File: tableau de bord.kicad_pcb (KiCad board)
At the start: 2 copper layers, 36.8 x 42.5 mm, 15 parts, among them J1 TS ON, J2 Alim, J3 R2D, J4 Potentiometre, J5 commande onduleur, U1 L7805

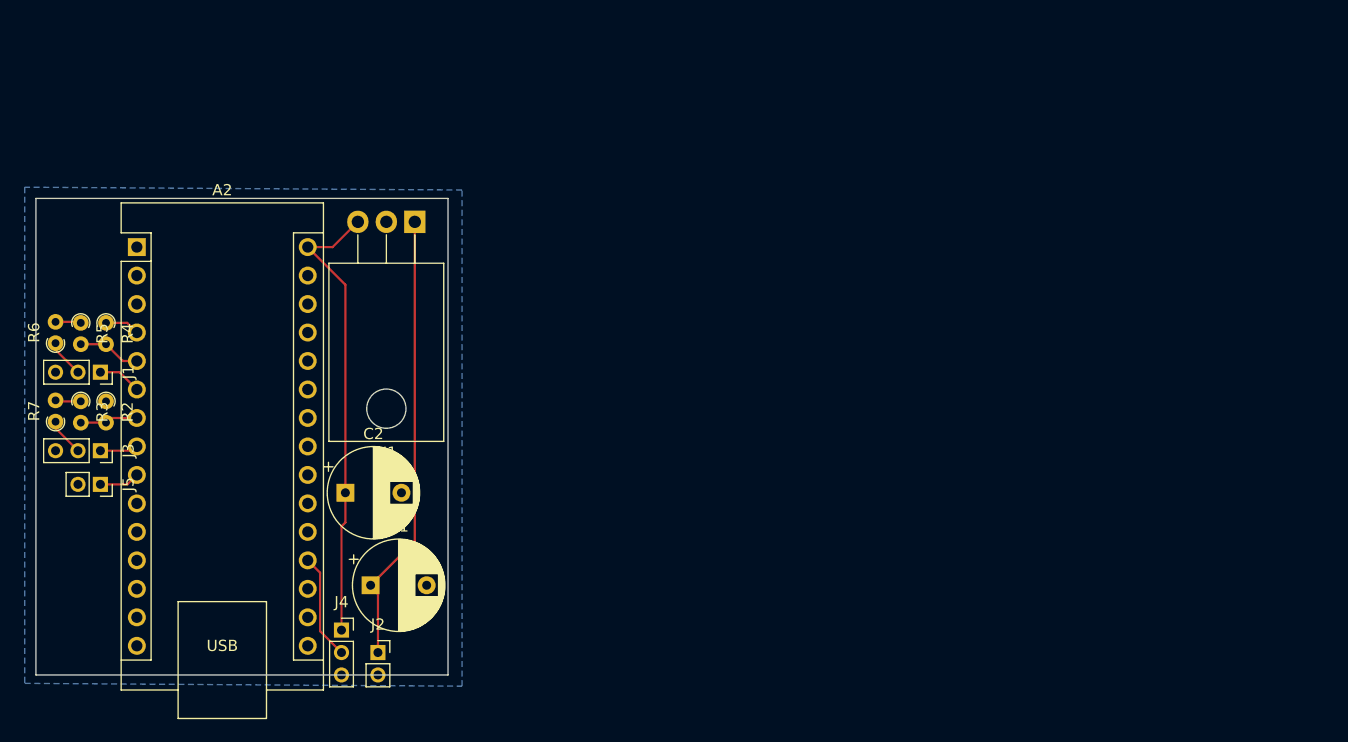
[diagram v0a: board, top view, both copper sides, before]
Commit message: Version 2:
- ajout de mosfet pour commander les relais.
- mise en forme des connecteurs
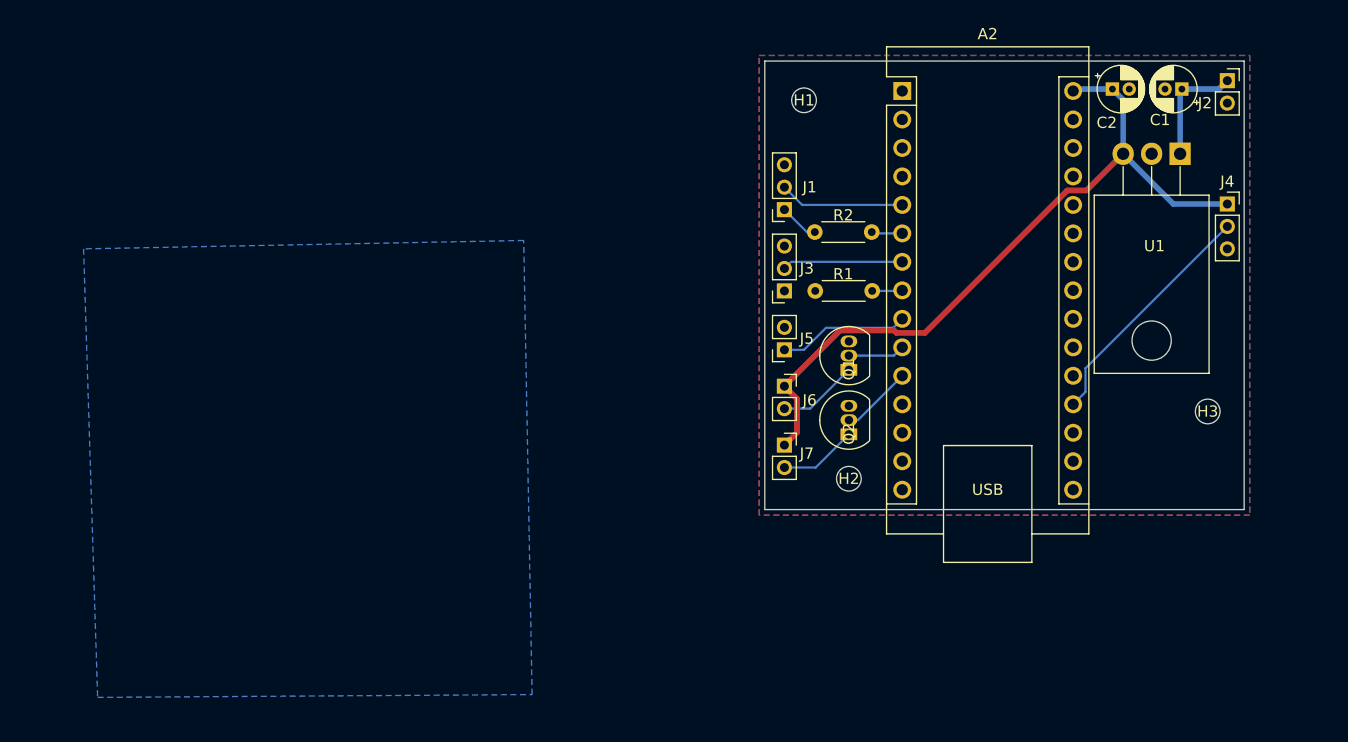
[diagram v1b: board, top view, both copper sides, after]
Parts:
- removed R3, R5: 47k, Resistor_THT:R_Axial_DIN0204_L3.6mm_D1.6mm_P1.90mm_Vertical
- removed R4, R6, R7: 4.7k, Resistor_THT:R_Axial_DIN0204_L3.6mm_D1.6mm_P1.90mm_Vertical
- added H1: MountingHole, MountingHole:MountingHole_2.2mm_M2, F.Cu at (139.5, 86.8)
- added H2: MountingHole, MountingHole:MountingHole_2.2mm_M2, F.Cu at (143.5, 120.5)
- added H3: MountingHole, MountingHole:MountingHole_2.2mm_M2, F.Cu at (175.5, 114.5)
- added J6: relais TS, Connector_PinSocket_2.00mm:PinSocket_1x02_P2.00mm_Vertical, F.Cu at (137.8, 112.2)
- added J7: relais R2D, Connector_PinSocket_2.00mm:PinSocket_1x02_P2.00mm_Vertical, F.Cu at (137.8, 117.5)
- added Q1: BS108, Package_TO_SOT_THT:TO-92_Inline, F.Cu at (143.5, 110.8)
- added Q2: BS108, Package_TO_SOT_THT:TO-92_Inline, F.Cu at (143.5, 116.5)
- added R1: 4.7k, Resistor_THT:R_Axial_DIN0204_L3.6mm_D1.6mm_P5.08mm_Horizontal, F.Cu at (140.5, 103.8)
- C1, C2: footprint Capacitor_THT:CP_Radial_D8.0mm_P5.00mm -> Capacitor_THT:CP_Radial_D4.0mm_P1.50mm
- R2: footprint Resistor_THT:R_Axial_DIN0204_L3.6mm_D1.6mm_P1.90mm_Vertical -> Resistor_THT:R_Axial_DIN0204_L3.6mm_D1.6mm_P5.08mm_Horizontal
- moved J2 91.3 mm to (177.2, 85.0)
- moved J4 87.7 mm to (177.2, 96.0)
- moved C1 84.8 mm to (173.2, 85.8), turned to 180 degrees
- moved C2 77.3 mm to (167.0, 85.8)
- moved A2 69.7 mm to (148.3, 85.9)
- moved U1 68.5 mm to (173.0, 91.5)
- moved R2 65.0 mm to (140.5, 98.5), turned to 0 degrees
- moved J1 62.7 mm to (137.8, 96.5), turned to 180 degrees
- moved J3 62.6 mm to (137.8, 103.8), turned to 180 degrees
- moved J5 62.2 mm to (137.8, 109.0), turned to 180 degrees
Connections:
- A2 pad 10: unconnected-(A2-D7-Pad10) -> Net-(A2-D7)
- A2 pad 11: unconnected-(A2-D8-Pad11) -> Net-(A2-D8)
- A2 pad 5: Net-(A2-D2) -> /ts button
- A2 pad 6: /led ts -> Net-(A2-D3)
- A2 pad 7: Net-(A2-D4) -> /r2d button
- A2 pad 8: /led r2d -> Net-(A2-D5)
- J1 pad 2: /ts -> /ts button
- J3 pad 2: /r2d -> /r2d button
- R2 pad 1: GND -> /led ts
- R2 pad 2: Net-(A2-D4) -> Net-(A2-D3)
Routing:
- net +12V: track 40.3 -> 10.2 mm
- net VCC: track 41.1 -> 66.0 mm
- net /vitesse: track 9.47 -> 21.6 mm
- net /ts button: track 0.00 -> 11.2 mm
- net /r2d button: track 0.00 -> 10.8 mm
- net /commande: track 3.60 -> 11.7 mm
- net Net-(J6-Pin_2): track 0.00 -> 7.18 mm
- net Net-(J7-Pin_2): track 0.00 -> 6.98 mm
- net Net-(A2-D8): track 0.00 -> 6.40 mm
- net Net-(A2-D2): track 5.62 -> 0.00 mm
- net Net-(A2-D4): track 5.17 -> 0.00 mm
- net Net-(A2-D7): track 0.00 -> 5.07 mm
- net /ts: track 3.42 -> 0.00 mm
- net /r2d: track 3.42 -> 0.00 mm
- net /led r2d: track 3.41 -> 0.00 mm
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- added copper zone on F.Cu, net GND
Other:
- board size 36.8 x 42.5 mm -> 42.8 x 40 mm

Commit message: Nouveaux connecteurs, amélioration de la qualité
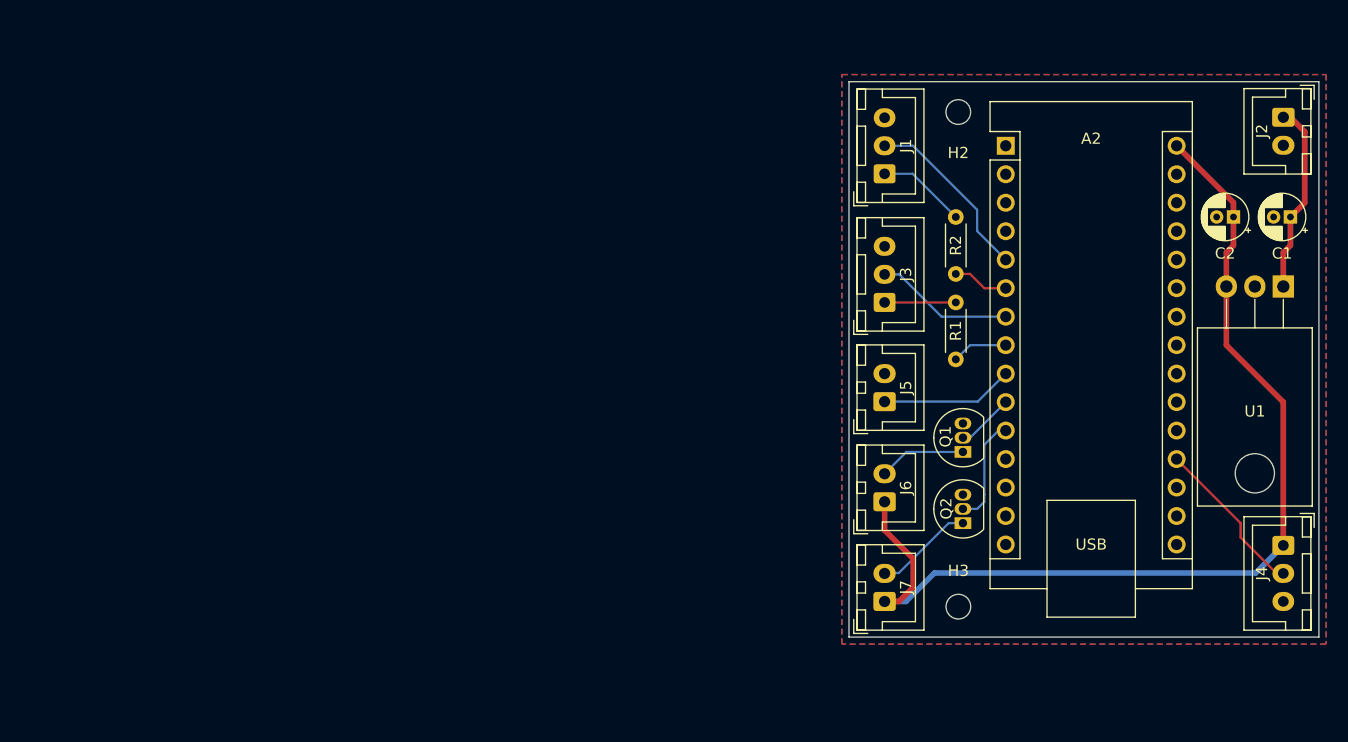
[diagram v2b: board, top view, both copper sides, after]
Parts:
- removed H1: MountingHole, MountingHole:MountingHole_2.2mm_M2
- J1, J3, J4: footprint Connector_PinSocket_2.00mm:PinSocket_1x03_P2.00mm_Vertical -> Connector_JST:JST_XH_B3B-XH-A_1x03_P2.50mm_Vertical
- J2, J5, J6, J7: footprint Connector_PinSocket_2.00mm:PinSocket_1x02_P2.00mm_Vertical -> Connector_JST:JST_XH_B2B-XH-A_1x02_P2.50mm_Vertical
- moved H2 34.1 mm to (153.3, 87.8)
- moved J4 30.9 mm to (182.2, 126.4), turned to -90 degrees
- moved H3 28.2 mm to (153.3, 131.9)
- moved J7 16.6 mm to (146.7, 131.4), turned to 90 degrees
- moved C2 15.7 mm to (177.8, 97.2), turned to 180 degrees
- moved U1 15.0 mm to (182.2, 103.4)
- moved C1 15.0 mm to (182.9, 97.2)
- moved J6 13.6 mm to (146.7, 122.6), turned to 90 degrees
- moved Q2 12.9 mm to (153.7, 124.5)
- moved R2 12.6 mm to (153.0, 97.2), turned to -90 degrees
- moved R1 12.6 mm to (153.0, 104.8), turned to -90 degrees
- moved Q1 12.5 mm to (153.7, 118.1)
- moved A2 10.4 mm to (157.5, 90.8)
- moved J5 10.1 mm to (146.7, 113.6), turned to 90 degrees
- moved J1 9.49 mm to (146.7, 93.3), turned to 90 degrees
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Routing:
- net VCC: track 66.0 -> 89.5 mm
- net /vitesse: track 21.6 -> 14.5 mm
- net /led r2d: track 0.00 -> 6.35 mm
- net +12V: track 10.2 -> 15.6 mm
- net /ts button: track 11.2 -> 16.1 mm
- net /led ts: track 3.54 -> 7.94 mm
- net Net-(A2-D8): track 6.40 -> 9.69 mm
- net Net-(A2-D3): track 2.77 -> 4.98 mm
- net Net-(J7-Pin_2): track 6.98 -> 8.83 mm
- net Net-(A2-D5): track 3.33 -> 4.98 mm
- net /r2d button: track 10.8 -> 12.4 mm
- net Net-(J6-Pin_2): track 7.18 -> 7.79 mm
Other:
- board size 42.8 x 40 mm -> 41.9 x 49.5 mm

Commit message: Revert "Nouveaux connecteurs, amélioration de la qualité"
This reverts commit 7978c89d57e71e12e8c7bad613f2c47c352c5b43.
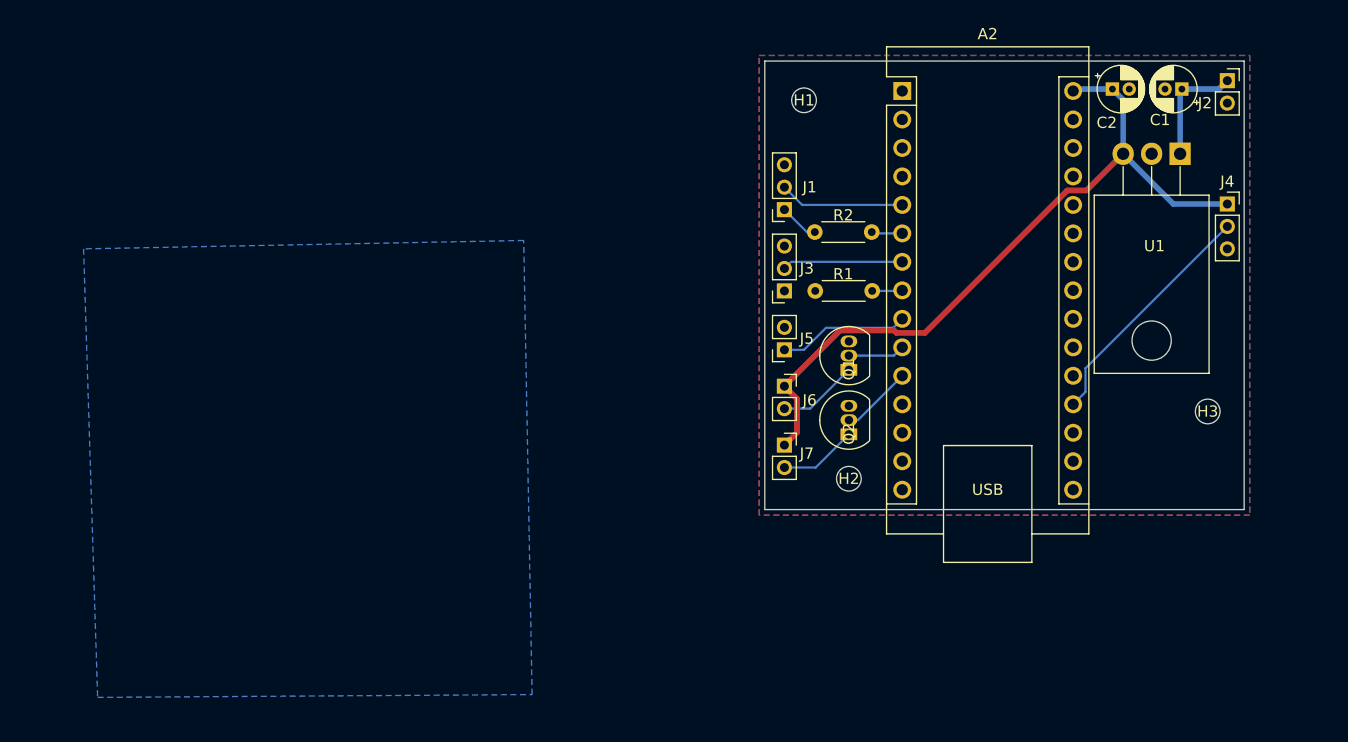
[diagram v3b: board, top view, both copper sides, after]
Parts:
- added H1: MountingHole, MountingHole:MountingHole_2.2mm_M2, F.Cu at (139.5, 86.8)
- J1, J3, J4: footprint Connector_JST:JST_XH_B3B-XH-A_1x03_P2.50mm_Vertical -> Connector_PinSocket_2.00mm:PinSocket_1x03_P2.00mm_Vertical
- J2, J5, J6, J7: footprint Connector_JST:JST_XH_B2B-XH-A_1x02_P2.50mm_Vertical -> Connector_PinSocket_2.00mm:PinSocket_1x02_P2.00mm_Vertical
- moved H2 34.1 mm to (143.5, 120.5)
- moved J4 30.9 mm to (177.2, 96.0), turned to 0 degrees
- moved H3 28.2 mm to (175.5, 114.5)
- moved J7 16.6 mm to (137.8, 117.5), turned to 0 degrees
- moved C2 15.7 mm to (167.0, 85.8), turned to 0 degrees
- moved U1 15.0 mm to (173.0, 91.5)
- moved C1 15.0 mm to (173.2, 85.8)
- moved J6 13.6 mm to (137.8, 112.2), turned to 0 degrees
- moved Q2 12.9 mm to (143.5, 116.5)
- moved R2 12.6 mm to (140.5, 98.5), turned to 0 degrees
- moved R1 12.6 mm to (140.5, 103.8), turned to 0 degrees
- moved Q1 12.5 mm to (143.5, 110.8)
- moved A2 10.4 mm to (148.3, 85.9)
- moved J5 10.1 mm to (137.8, 109.0), turned to 180 degrees
- moved J1 9.49 mm to (137.8, 96.5), turned to 180 degrees
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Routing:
- net VCC: track 89.5 -> 66.0 mm
- net /vitesse: track 14.5 -> 21.6 mm
- net /led r2d: track 6.35 -> 0.00 mm
- net +12V: track 15.6 -> 10.2 mm
- net /ts button: track 16.1 -> 11.2 mm
- net /led ts: track 7.94 -> 3.54 mm
- net Net-(A2-D8): track 9.69 -> 6.40 mm
- net Net-(A2-D3): track 4.98 -> 2.77 mm
- net Net-(J7-Pin_2): track 8.83 -> 6.98 mm
- net Net-(A2-D5): track 4.98 -> 3.33 mm
- net /r2d button: track 12.4 -> 10.8 mm
- net Net-(J6-Pin_2): track 7.79 -> 7.18 mm
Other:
- board size 41.9 x 49.5 mm -> 42.8 x 40 mm
